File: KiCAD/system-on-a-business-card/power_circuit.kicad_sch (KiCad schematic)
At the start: 13 parts, among them SW3 SW_DIP_x01, U4 ZD1117ILTRAD

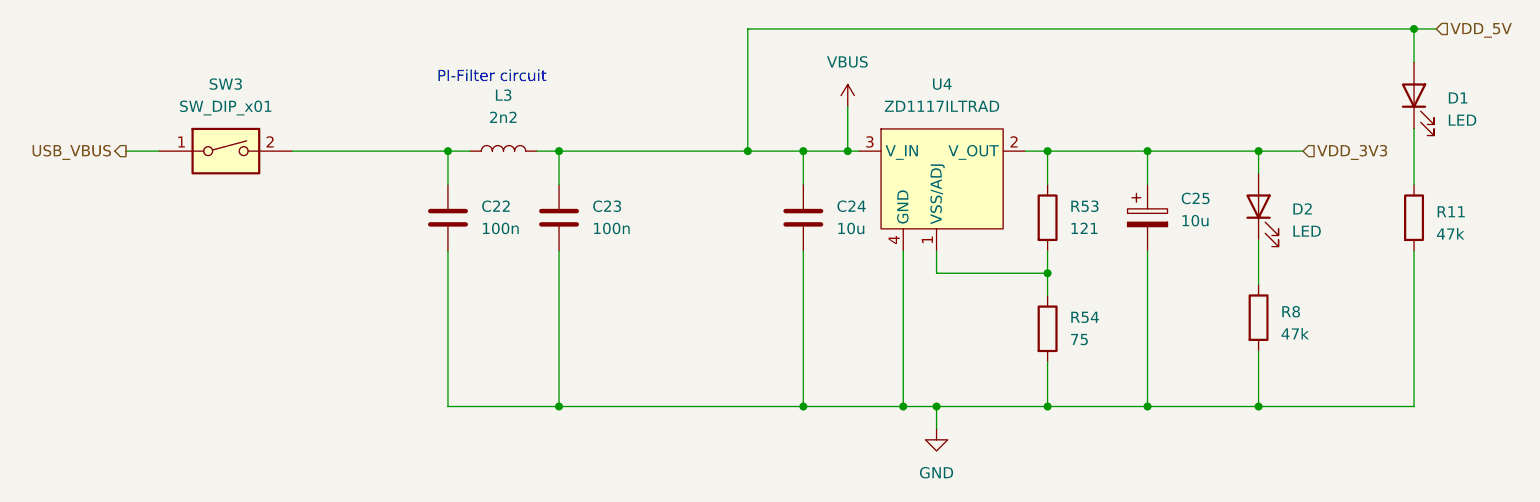
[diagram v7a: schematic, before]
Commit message: #10: removed on/off switch again, started working on layout
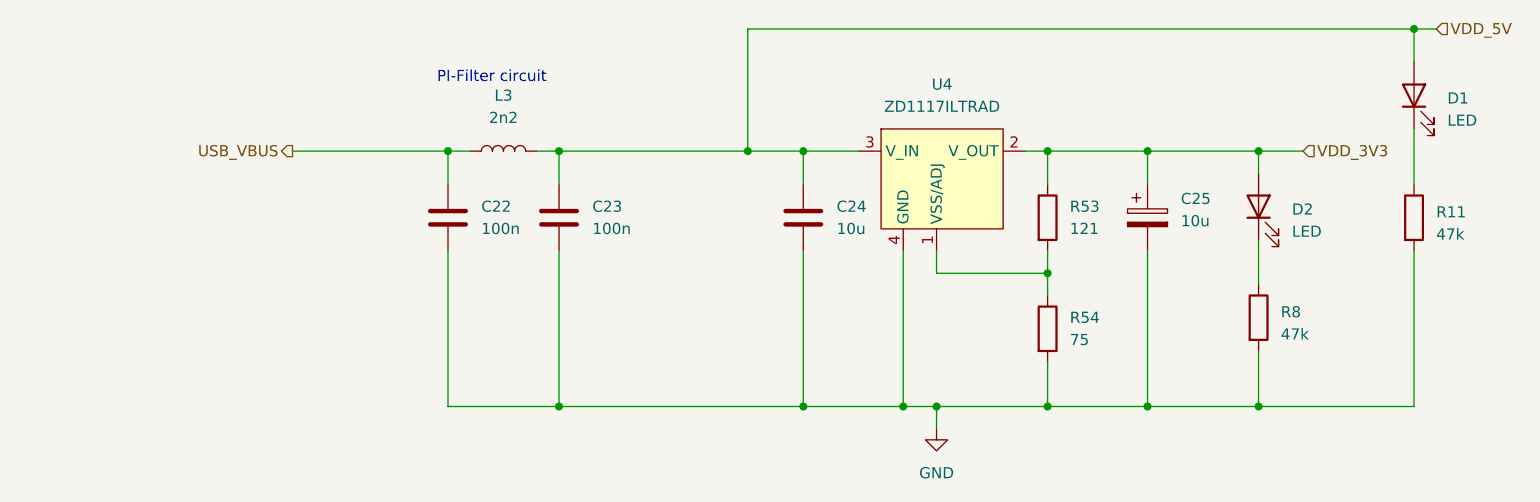
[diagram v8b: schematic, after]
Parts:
- removed SW3: SW_DIP_x01, symbol Switch:SW_DIP_x01
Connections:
- net USB_VBUS: now also C22.1, L3.1
- net VBUS renamed VDD_5V
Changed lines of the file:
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@@
   (junction (at 140.97 52.07) (diameter 0) (color 0 0 0 0)
   )
-  (junction (at 118.11 52.07) (diameter 0) (color 0 0 0 0)
-  )
   (junction (at 124.46 81.28) (diameter 0) (color 0 0 0 0)
   )
@@
     (stroke (width 0) (type default))
   )
-  (wire (pts (xy 118.11 52.07) (xy 119.38 52.07))
-    (stroke (width 0) (type default))
-  )
   (wire (pts (xy 85.09 63.5) (xy 85.09 81.28))
     (stroke (width 0) (type default))
@@
     (stroke (width 0) (type default))
   )
-  (wire (pts (xy 118.11 46.99) (xy 118.11 52.07))
-    (stroke (width 0) (type default))
-  )
   (wire (pts (xy 72.39 81.28) (xy 85.09 81.28))
     (stroke (width 0) (type default))
@@
     (stroke (width 0) (type default))
   )
-  (wire (pts (xy 35.56 52.07) (xy 39.37 52.07))
-    (stroke (width 0) (type default))
-  )
-  (wire (pts (xy 113.03 52.07) (xy 118.11 52.07))
+  (wire (pts (xy 113.03 52.07) (xy 119.38 52.07))
     (stroke (width 0) (type default))
   )
@@
     (effects (font (size 1.27 1.27)) (justify left))
   )
-  (hierarchical_label "USB_VBUS" (shape output) (at 35.56 52.07 180) (fields_autoplaced)
+  (hierarchical_label "USB_VBUS" (shape output) (at 54.61 52.07 180) (fields_autoplaced)
     (effects (font (size 1.27 1.27)) (justify right))
   )
@@
     )
   )
-  (symbol (lib_id "power:VBUS") (at 118.11 46.99 0) (unit 1)
-    (in_bom yes) (on_board yes) (dnp no) (fields_autoplaced)
-    (property "Reference" "#PWR026" (at 118.11 50.8 0)
-      (effects (font (size 1.27 1.27)) hide)
-    )
-    (property "Value" "VBUS" (at 118.11 41.91 0)
-      (effects (font (size 1.27 1.27)))
-    )
-    (property "Footprint" "" (at 118.11 46.99 0)
-      (effects (font (size 1.27 1.27)) hide)
-    )
-    (property "Datasheet" "" (at 118.11 46.99 0)
-      (effects (font (size 1.27 1.27)) hide)
-    )
-    (pin "1")
-    (instances
-      (project "system-on-a-business-card"
-        (path "/49855302-2ecc-4f42-8bbd-b9c2e284f529/eba2cd67-fe31-4e76-9673-7c97f7251114"
-          (reference "#PWR026") (unit 1)
-        )
-      )
-    )
-  )
   (symbol (lib_id "Device:C") (at 72.39 59.69 0) (unit 1)
     (in_bom yes) (on_board yes) (dnp no) (fields_autoplaced)
@@
         )
       )
-    )
-  )
-  (symbol (lib_id "Switch:SW_DIP_x01") (at 46.99 52.07 0) (unit 1)
-    (in_bom yes) (on_board yes) (dnp no) (fields_autoplaced)
-    (property "Reference" "SW3" (at 46.99 44.45 0)
-      (effects (font (size 1.27 1.27)))
-    )
-    (property "Value" "SW_DIP_x01" (at 46.99 46.99 0)
-      (effects (font (size 1.27 1.27)))
-    )
-    (property "Footprint" "" (at 46.99 52.07 0)
-      (effects (font (size 1.27 1.27)) hide)
-    )
-    (property "Datasheet" "~" (at 46.99 52.07 0)
-      (effects (font (size 1.27 1.27)) hide)
-    )
-    (pin "1")
-    (pin "2")
-    (instances
-      (project "system-on-a-business-card"
-        (path "/49855302-2ecc-4f42-8bbd-b9c2e284f529/eba2cd67-fe31-4e76-9673-7c97f7251114"
-          (reference "SW3") (unit 1)
-        )
-      )
